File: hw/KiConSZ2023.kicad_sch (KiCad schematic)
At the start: 0 parts

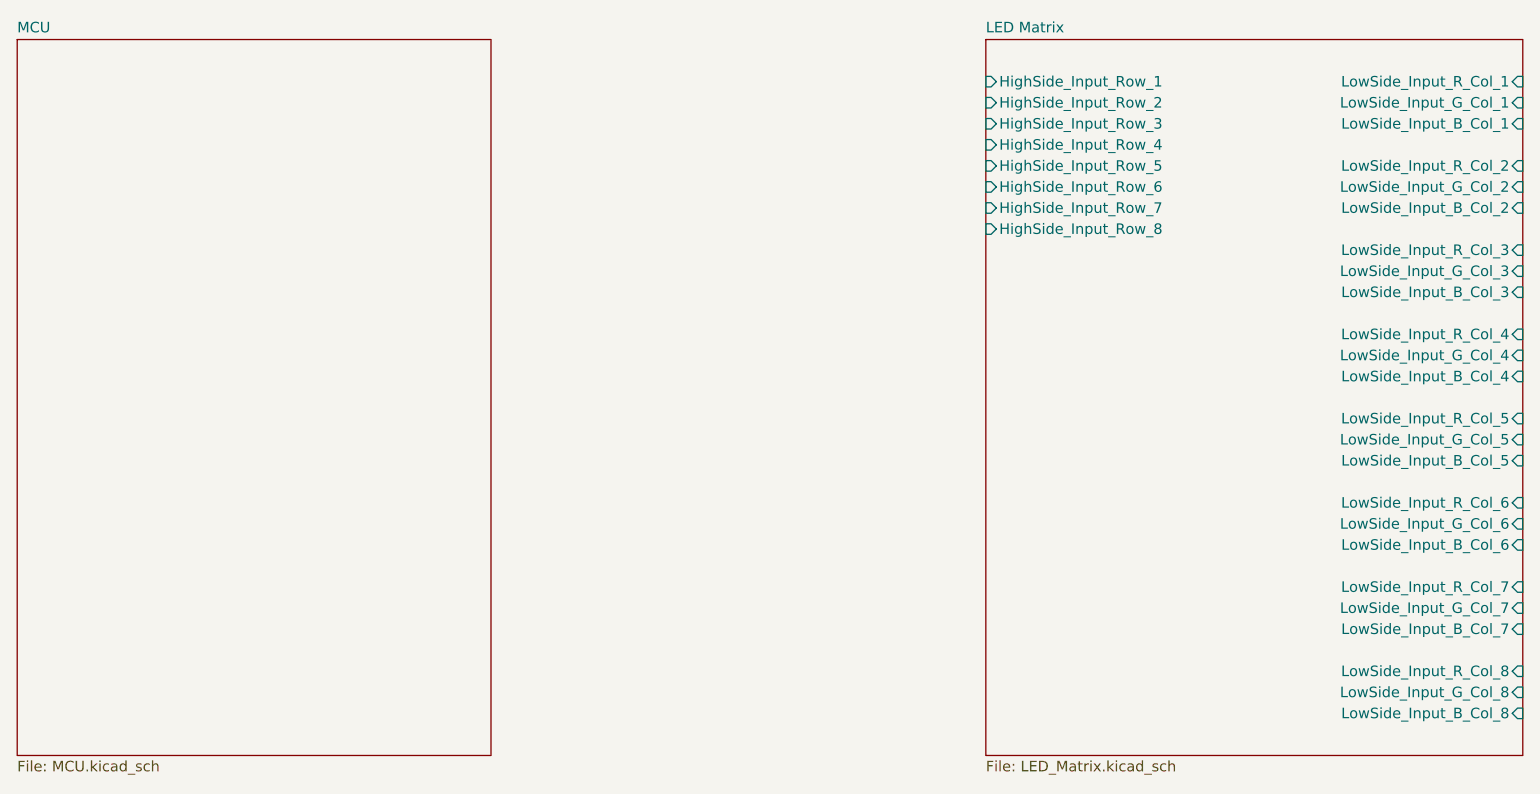
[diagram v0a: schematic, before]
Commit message: updated pin connections
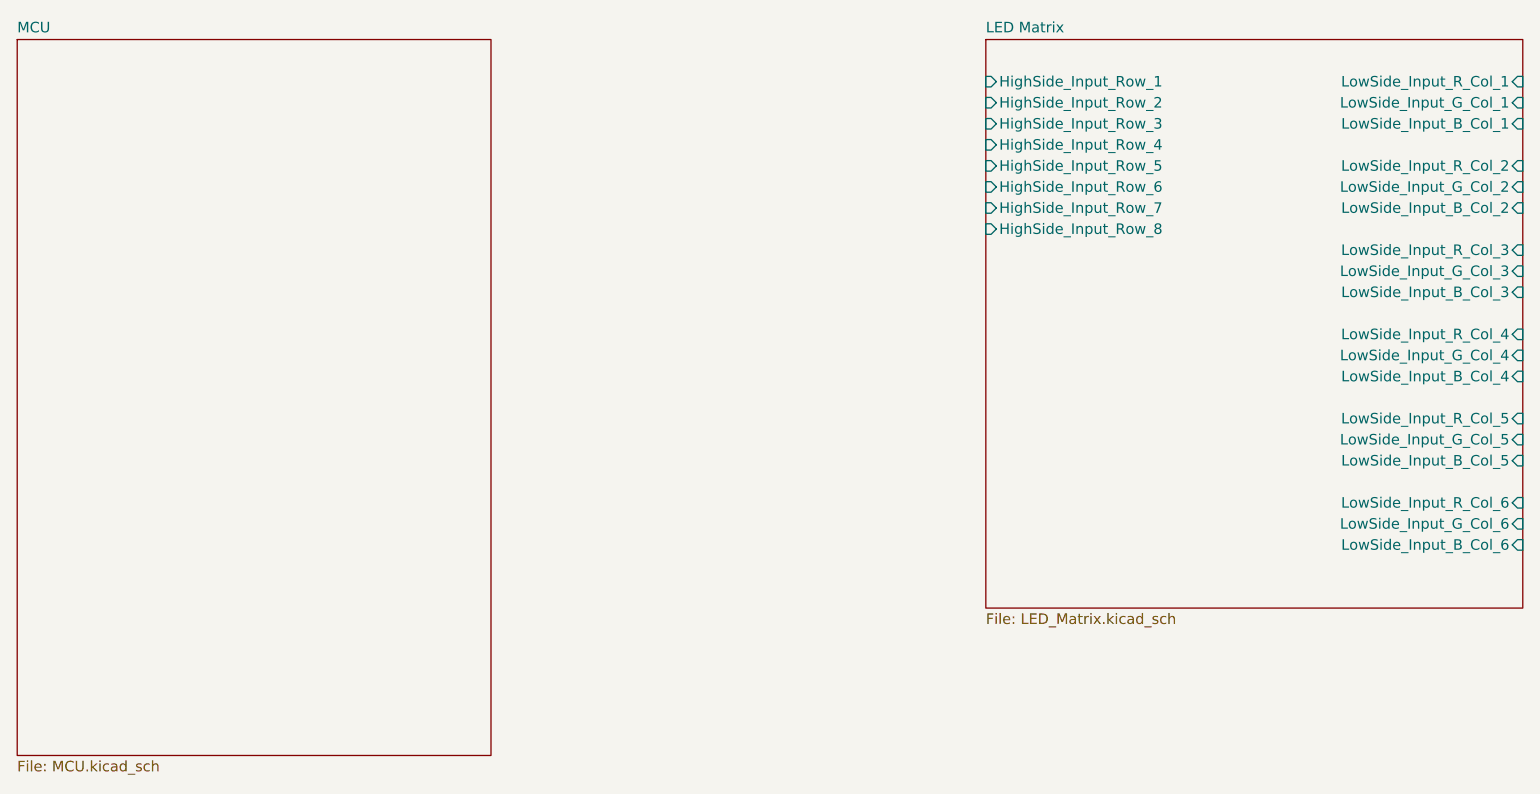
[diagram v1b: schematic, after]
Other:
- sheet LED Matrix ports: added none; removed LowSide_Input_B_Col_7, LowSide_Input_B_Col_8, LowSide_Input_G_Col_7, LowSide_Input_G_Col_8, LowSide_Input_R_Col_7, LowSide_Input_R_Col_8
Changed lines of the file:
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@@
 (kicad_sch (version 20230121) (generator eeschema)
   (paper "A4")
-  (sheet (at 177.8 48.26) (size 64.77 86.36) (fields_autoplaced)
+  (sheet (at 177.8 48.26) (size 64.77 68.58) (fields_autoplaced)
     (stroke (width 0.1524) (type solid))
     (fill (color 0 0 0 0.0000))
@@
       (effects (font (size 1.27 1.27)) (justify left bottom))
     )
-    (property "Sheetfile" "LED_Matrix.kicad_sch" (at 177.8 135.2046 0)
+    (property "Sheetfile" "LED_Matrix.kicad_sch" (at 177.8 117.4246 0)
       (effects (font (size 1.27 1.27)) (justify left top))
     )
@@
       (effects (font (size 1.27 1.27)) (justify right))
     )
-    (pin "LowSide_Input_R_Col_7" input (at 242.57 114.3 0)
-      (effects (font (size 1.27 1.27)) (justify right))
-    )
-    (pin "LowSide_Input_G_Col_7" input (at 242.57 116.84 0)
-      (effects (font (size 1.27 1.27)) (justify right))
-    )
-    (pin "LowSide_Input_B_Col_7" input (at 242.57 119.38 0)
-      (effects (font (size 1.27 1.27)) (justify right))
-    )
-    (pin "LowSide_Input_R_Col_8" input (at 242.57 124.46 0)
-      (effects (font (size 1.27 1.27)) (justify right))
-    )
-    (pin "LowSide_Input_G_Col_8" input (at 242.57 127 0)
-      (effects (font (size 1.27 1.27)) (justify right))
-    )
-    (pin "LowSide_Input_B_Col_8" input (at 242.57 129.54 0)
-      (effects (font (size 1.27 1.27)) (justify right))
-    )

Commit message: added more connections
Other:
- sheet MCU ports: added DISP_MISO, DISP_MOSI, DISP_SCK, DISP_~{SS}, HighSide_Input_Row_1, HighSide_Input_Row_2, HighSide_Input_Row_3, HighSide_Input_Row_4, HighSide_Input_Row_5, HighSide_Input_Row_6, HighSide_Input_Row_7, HighSide_Input_Row_8, I2C1_SCL, I2C1_SDA, LowSide_Input_B_Col_1, LowSide_Input_B_Col_2, LowSide_Input_B_Col_3, LowSide_Input_B_Col_4, LowSide_Input_B_Col_5, LowSide_Input_B_Col_6, LowSide_Input_G_Col_1, LowSide_Input_G_Col_2, LowSide_Input_G_Col_3, LowSide_Input_G_Col_4, LowSide_Input_G_Col_5, LowSide_Input_G_Col_6, LowSide_Input_R_Col_1, LowSide_Input_R_Col_2, LowSide_Input_R_Col_3, LowSide_Input_R_Col_4, LowSide_Input_R_Col_5, LowSide_Input_R_Col_6, SWDCLK, SWDIO, USART_RX, USART_TX, USB_DN, USB_DP, VDD; removed none
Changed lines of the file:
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@@
       (effects (font (size 1.27 1.27)) (justify left top))
+    )
+    (pin "HighSide_Input_Row_4" input (at 118.11 60.96 0)
+      (effects (font (size 1.27 1.27)) (justify right))
+    )
+    (pin "HighSide_Input_Row_7" input (at 118.11 68.58 0)
+      (effects (font (size 1.27 1.27)) (justify right))
+    )
+    (pin "HighSide_Input_Row_6" input (at 118.11 66.04 0)
+      (effects (font (size 1.27 1.27)) (justify right))
+    )
+    (pin "HighSide_Input_Row_5" input (at 118.11 63.5 0)
+      (effects (font (size 1.27 1.27)) (justify right))
+    )
+    (pin "HighSide_Input_Row_8" input (at 118.11 71.12 0)
+      (effects (font (size 1.27 1.27)) (justify right))
+    )
+    (pin "HighSide_Input_Row_3" input (at 118.11 58.42 0)
+      (effects (font (size 1.27 1.27)) (justify right))
+    )
+    (pin "HighSide_Input_Row_2" input (at 118.11 55.88 0)
+      (effects (font (size 1.27 1.27)) (justify right))
+    )
+    (pin "HighSide_Input_Row_1" input (at 118.11 53.34 0)
+      (effects (font (size 1.27 1.27)) (justify right))
+    )
+    (pin "VDD" input (at 60.96 50.8 180)
+      (effects (font (size 1.27 1.27)) (justify left))
+    )
+    (pin "LowSide_Input_G_Col_3" input (at 118.11 93.98 0)
+      (effects (font (size 1.27 1.27)) (justify right))
+    )
+    (pin "LowSide_Input_B_Col_4" input (at 118.11 104.14 0)
+      (effects (font (size 1.27 1.27)) (justify right))
+    )
+    (pin "LowSide_Input_B_Col_3" input (at 118.11 96.52 0)
+      (effects (font (size 1.27 1.27)) (justify right))
+    )
+    (pin "LowSide_Input_R_Col_4" input (at 118.11 99.06 0)
+      (effects (font (size 1.27 1.27)) (justify right))
+    )
+    (pin "LowSide_Input_G_Col_4" input (at 118.11 101.6 0)
+      (effects (font (size 1.27 1.27)) (justify right))
+    )
+    (pin "LowSide_Input_R_Col_3" input (at 118.11 91.44 0)
+      (effects (font (size 1.27 1.27)) (justify right))
+    )
+    (pin "LowSide_Input_G_Col_2" input (at 118.11 86.36 0)
+      (effects (font (size 1.27 1.27)) (justify right))
+    )
+    (pin "LowSide_Input_B_Col_2" input (at 118.11 88.9 0)
+      (effects (font (size 1.27 1.27)) (justify right))
+    )
+    (pin "LowSide_Input_R_Col_2" input (at 118.11 83.82 0)
+      (effects (font (size 1.27 1.27)) (justify right))
+    )
+    (pin "LowSide_Input_B_Col_1" input (at 118.11 81.28 0)
+      (effects (font (size 1.27 1.27)) (justify right))
+    )
+    (pin "LowSide_Input_G_Col_1" input (at 118.11 78.74 0)
+      (effects (font (size 1.27 1.27)) (justify right))
+    )
+    (pin "LowSide_Input_R_Col_1" input (at 118.11 76.2 0)
+      (effects (font (size 1.27 1.27)) (justify right))
+    )
+    (pin "LowSide_Input_R_Col_5" input (at 118.11 106.68 0)
+      (effects (font (size 1.27 1.27)) (justify right))
+    )
+    (pin "LowSide_Input_G_Col_5" input (at 118.11 109.22 0)
+      (effects (font (size 1.27 1.27)) (justify right))
+    )
+    (pin "LowSide_Input_R_Col_6" input (at 118.11 114.3 0)
+      (effects (font (size 1.27 1.27)) (justify right))
+    )
+    (pin "LowSide_Input_B_Col_5" input (at 118.11 111.76 0)
+      (effects (font (size 1.27 1.27)) (justify right))
+    )
+    (pin "LowSide_Input_G_Col_6" input (at 118.11 116.84 0)
+      (effects (font (size 1.27 1.27)) (justify right))
+    )
+    (pin "LowSide_Input_B_Col_6" input (at 118.11 119.38 0)
+      (effects (font (size 1.27 1.27)) (justify right))
+    )
+    (pin "I2C1_SCL" output (at 60.96 55.88 180)
+      (effects (font (size 1.27 1.27)) (justify left))
+    )
+    (pin "I2C1_SDA" bidirectional (at 60.96 58.42 180)
+      (effects (font (size 1.27 1.27)) (justify left))
+    )
+    (pin "DISP_~{SS}" output (at 60.96 71.12 180)
+      (effects (font (size 1.27 1.27)) (justify left))
+    )
+    (pin "DISP_SCK" output (at 60.96 73.66 180)
+      (effects (font (size 1.27 1.27)) (justify left))
+    )
+    (pin "DISP_MOSI" output (at 60.96 76.2 180)
+      (effects (font (size 1.27 1.27)) (justify left))
+    )
+    (pin "DISP_MISO" input (at 60.96 78.74 180)
+      (effects (font (size 1.27 1.27)) (justify left))
+    )
+    (pin "USART_TX" output (at 60.96 63.5 180)
+      (effects (font (size 1.27 1.27)) (justify left))
+    )
+    (pin "USART_RX" input (at 60.96 66.04 180)
+      (effects (font (size 1.27 1.27)) (justify left))
+    )
+    (pin "SWDCLK" output (at 60.96 83.82 180)
+      (effects (font (size 1.27 1.27)) (justify left))
+    )
+    (pin "SWDIO" bidirectional (at 60.96 86.36 180)
+      (effects (font (size 1.27 1.27)) (justify left))
+    )
+    (pin "USB_DP" bidirectional (at 60.96 91.44 180)
+      (effects (font (size 1.27 1.27)) (justify left))
+    )
+    (pin "USB_DN" bidirectional (at 60.96 93.98 180)
+      (effects (font (size 1.27 1.27)) (justify left))
     )
     (instances
